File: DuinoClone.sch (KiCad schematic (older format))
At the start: 8 parts

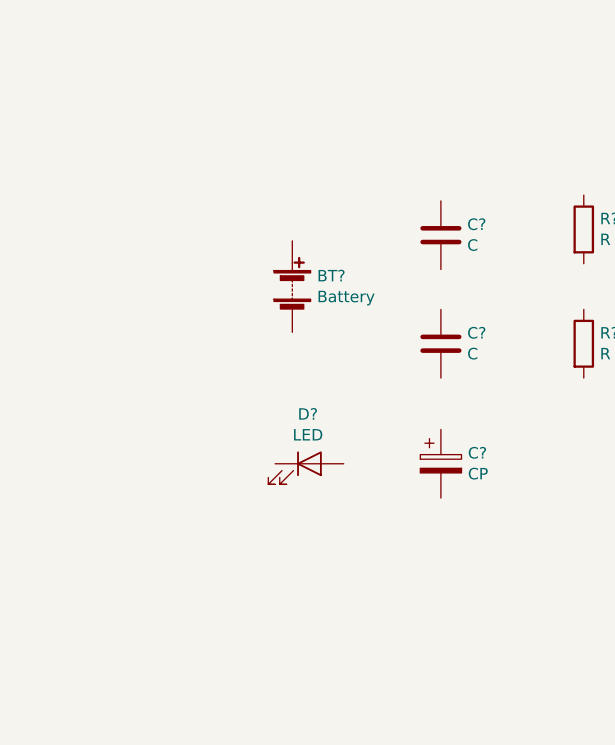
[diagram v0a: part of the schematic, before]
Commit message: Added symbol for Atmega328p-au
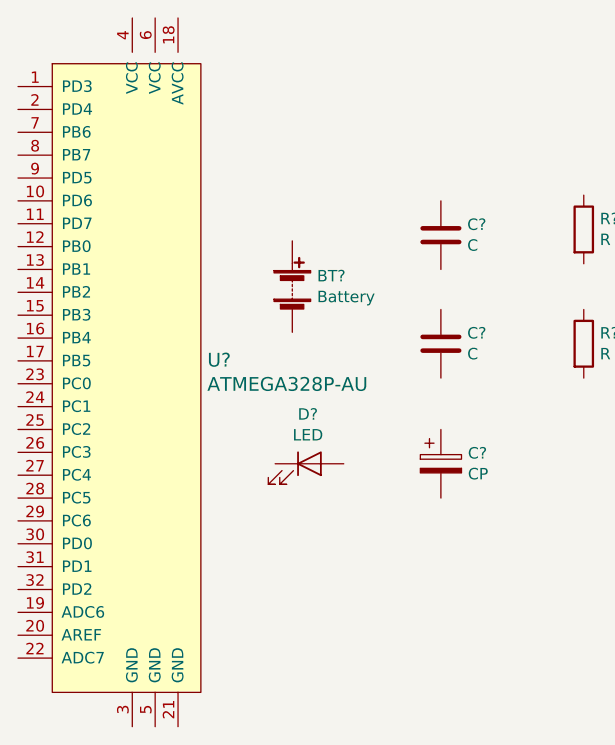
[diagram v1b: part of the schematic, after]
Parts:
- added U?: ATMEGA328P-AU, digikey-footprints:TQFP-32_7x7mm, symbol dk_Embedded-Microcontrollers:ATMEGA328P-AU
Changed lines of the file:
@@
 F1 "Connectors.sch" 50
 $EndSheet
+$Comp
+L dk_Embedded-Microcontrollers:ATMEGA328P-AU U?
+U 1 1 5CE4135D
+P 3975 4000
+F 0 "U?" H 4303 4103 60  0000 L CNN
+F 1 "ATMEGA328P-AU" H 4303 3997 60  0000 L CNN
+F 2 "digikey-footprints:TQFP-32_7x7mm" H 4175 4200 60  0001 L CNN
+F 3 "http://www.microchip.com/mymicrochip/filehandler.aspx?ddocname=en589968" H 4175 4300 60  0001 L CNN
+F 4 "ATMEGA328P-AU-ND" H 4175 4400 60  0001 L CNN "Digi-Key_PN"
+F 5 "ATMEGA328P-AU" H 4175 4500 60  0001 L CNN "MPN"
+F 6 "Integrated Circuits (ICs)" H 4175 4600 60  0001 L CNN "Category"
+F 7 "Embedded - Microcontrollers" H 4175 4700 60  0001 L CNN "Family"
+F 8 "http://www.microchip.com/mymicrochip/filehandler.aspx?ddocname=en589968" H 4175 4800 60  0001 L CNN "DK_Datasheet_Link"
+F 9 "/product-detail/en/microchip-technology/ATMEGA328P-AU/ATMEGA328P-AU-ND/1832260" H 4175 4900 60  0001 L CNN "DK_Detail_Page"
+F 10 "IC MCU 8BIT 32KB FLASH 32TQFP" H 4175 5000 60  0001 L CNN "Description"
+F 11 "Microchip Technology" H 4175 5100 60  0001 L CNN "Manufacturer"
+F 12 "Active" H 4175 5200 60  0001 L CNN "Status"
+	1    3975 4000
+	1    0    0    -1
+$EndComp
 $EndSCHEMATC

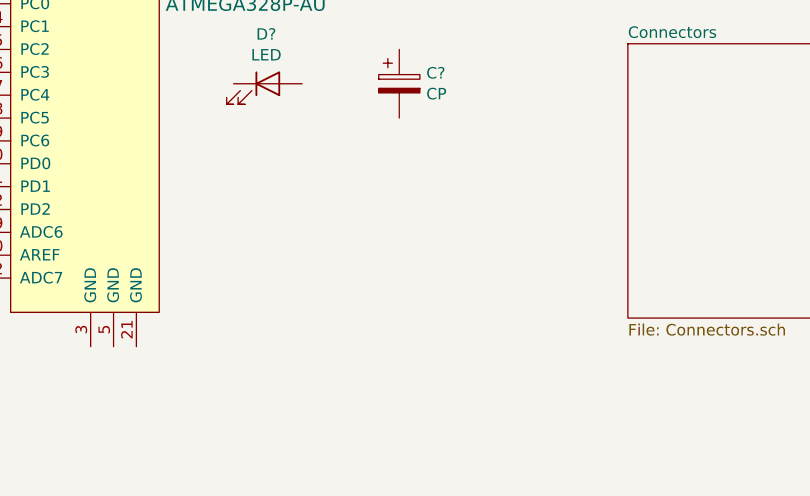
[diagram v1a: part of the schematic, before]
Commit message: Added clock IC custom symbol
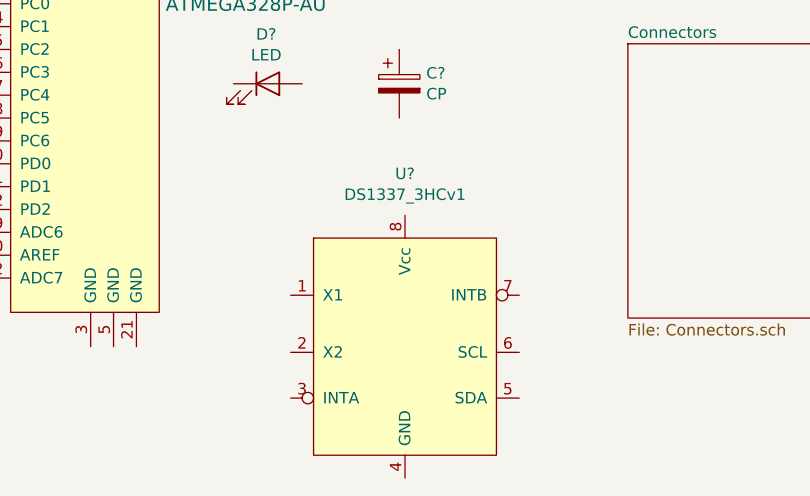
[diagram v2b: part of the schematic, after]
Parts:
- added U?: DS1337_3HCv1, symbol DuinoClone:DS1337_3HCv1
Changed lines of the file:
@@
+	1    0    0    -1
+$EndComp
+$Comp
+L DuinoClone:DS1337_3HCv1 U?
+U 1 1 5CE464AF
+P 5350 5475
+F 0 "U?" H 5350 6206 50  0000 C CNN
+F 1 "DS1337_3HCv1" H 5350 6115 50  0000 C CNN
+F 2 "" H 5700 6025 50  0001 C CNN
+F 3 "http://www.farnell.com/datasheets/74348.pdf" H 5700 6025 50  0001 C CNN
+	1    5350 5475
 	1    0    0    -1
 $EndComp

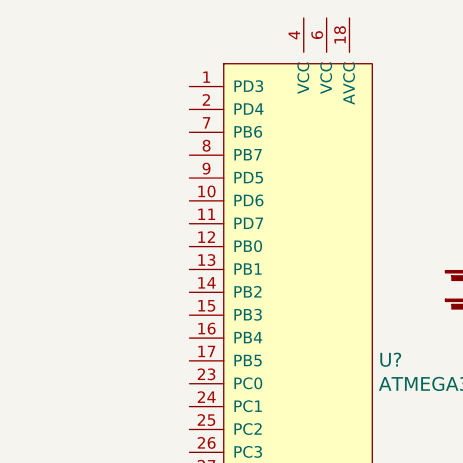
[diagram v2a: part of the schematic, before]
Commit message: Added crystal symbols to schematic
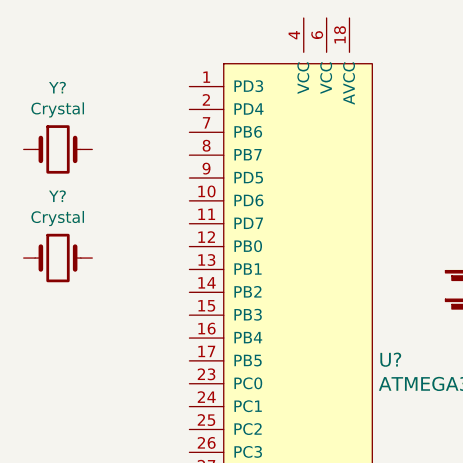
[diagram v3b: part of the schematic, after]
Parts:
- added Y? (x2): Crystal, symbol Device:Crystal
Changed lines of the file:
@@
+	1    0    0    -1
+$EndComp
+$Comp
+L Device:Crystal Y?
+U 1 1 5CE47483
+P 2900 2975
+F 0 "Y?" H 2900 3243 50  0000 C CNN
+F 1 "Crystal" H 2900 3152 50  0000 C CNN
+F 2 "" H 2900 2975 50  0001 C CNN
+F 3 "~" H 2900 2975 50  0001 C CNN
+	1    2900 2975
+	1    0    0    -1
+$EndComp
+$Comp
+L Device:Crystal Y?
+U 1 1 5CE4858A
+P 2900 3450
+F 0 "Y?" H 2900 3718 50  0000 C CNN
+F 1 "Crystal" H 2900 3627 50  0000 C CNN
+F 2 "" H 2900 3450 50  0001 C CNN
+F 3 "~" H 2900 3450 50  0001 C CNN
+	1    2900 3450
 	1    0    0    -1
 $EndComp

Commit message: Arranged symbols
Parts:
- added U?: 24LC1025, symbol Memory_EEPROM:24LC1025
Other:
- moved on the sheet: BT?, C?, D?, R?, U?, Y?
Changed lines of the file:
@@
 L Device:Battery BT?
 U 1 1 5CE2F41C
-P 4675 3575
-F 0 "BT?" H 4783 3621 50  0000 L CNN
-F 1 "Battery" H 4783 3530 50  0000 L CNN
-F 2 "" V 4675 3635 50  0001 C CNN
-F 3 "~" V 4675 3635 50  0001 C CNN
-	1    4675 3575
+P 8200 2275
+F 0 "BT?" H 8308 2321 50  0000 L CNN
+F 1 "Battery" H 8308 2230 50  0000 L CNN
+F 2 "" V 8200 2335 50  0001 C CNN
+F 3 "~" V 8200 2335 50  0001 C CNN
+	1    8200 2275
 	1    0    0    -1
 $EndComp
@@
 L Device:C C?
 U 1 1 5CE30EAD
-P 5325 3350
-F 0 "C?" H 5440 3396 50  0000 L CNN
-F 1 "C" H 5440 3305 50  0000 L CNN
-F 2 "" H 5363 3200 50  0001 C CNN
-F 3 "~" H 5325 3350 50  0001 C CNN
-	1    5325 3350
+P 4050 2400
+F 0 "C?" H 4165 2446 50  0000 L CNN
+F 1 "C" H 4165 2355 50  0000 L CNN
+F 2 "" H 4088 2250 50  0001 C CNN
+F 3 "~" H 4050 2400 50  0001 C CNN
+	1    4050 2400
 	1    0    0    -1
 $EndComp
@@
 L Device:C C?
 U 1 1 5CE31ACC
-P 5325 3825
-F 0 "C?" H 5440 3871 50  0000 L CNN
-F 1 "C" H 5440 3780 50  0000 L CNN
-F 2 "" H 5363 3675 50  0001 C CNN
-F 3 "~" H 5325 3825 50  0001 C CNN
-	1    5325 3825
+P 4050 2875
+F 0 "C?" H 4165 2921 50  0000 L CNN
+F 1 "C" H 4165 2830 50  0000 L CNN
+F 2 "" H 4088 2725 50  0001 C CNN
+F 3 "~" H 4050 2875 50  0001 C CNN
+	1    4050 2875
 	1    0    0    -1
 $EndComp
@@
 L Device:CP C?
 U 1 1 5CE322B6
-P 5325 4350
-F 0 "C?" H 5443 4396 50  0000 L CNN
-F 1 "CP" H 5443 4305 50  0000 L CNN
-F 2 "" H 5363 4200 50  0001 C CNN
-F 3 "~" H 5325 4350 50  0001 C CNN
-	1    5325 4350
+P 8525 3000
+F 0 "C?" H 8643 3046 50  0000 L CNN
+F 1 "CP" H 8643 2955 50  0000 L CNN
+F 2 "" H 8563 2850 50  0001 C CNN
+F 3 "~" H 8525 3000 50  0001 C CNN
+	1    8525 3000
 	1    0    0    -1
 $EndComp
@@
 L Device:LED D?
 U 1 1 5CE330B4
-P 4750 4350
-F 0 "D?" H 4743 4566 50  0000 C CNN
-F 1 "LED" H 4743 4475 50  0000 C CNN
-F 2 "" H 4750 4350 50  0001 C CNN
-F 3 "~" H 4750 4350 50  0001 C CNN
-	1    4750 4350
+P 4800 3275
+F 0 "D?" H 4793 3491 50  0000 C CNN
+F 1 "LED" H 4793 3400 50  0000 C CNN
+F 2 "" H 4800 3275 50  0001 C CNN
+F 3 "~" H 4800 3275 50  0001 C CNN
+	1    4800 3275
 	1    0    0    -1
 $EndComp
@@
 L Device:R R?
 U 1 1 5CE33F79
-P 5950 3325
-F 0 "R?" H 6020 3371 50  0000 L CNN
-F 1 "R" H 6020 3280 50  0000 L CNN
-F 2 "" V 5880 3325 50  0001 C CNN
-F 3 "~" H 5950 3325 50  0001 C CNN
-	1    5950 3325
+P 4275 3450
+F 0 "R?" H 4345 3496 50  0000 L CNN
+F 1 "R" H 4345 3405 50  0000 L CNN
+F 2 "" V 4205 3450 50  0001 C CNN
+F 3 "~" H 4275 3450 50  0001 C CNN
+	1    4275 3450
 	1    0    0    -1
 $EndComp
@@
 L Device:R R?
 U 1 1 5CE34AF5
-P 5950 3825
-F 0 "R?" H 6020 3871 50  0000 L CNN
-F 1 "R" H 6020 3780 50  0000 L CNN
-F 2 "" V 5880 3825 50  0001 C CNN
-F 3 "~" H 5950 3825 50  0001 C CNN
-	1    5950 3825
+P 4650 4775
+F 0 "R?" H 4720 4821 50  0000 L CNN
+F 1 "R" H 4720 4730 50  0000 L CNN
+F 2 "" V 4580 4775 50  0001 C CNN
+F 3 "~" H 4650 4775 50  0001 C CNN
+	1    4650 4775
 	1    0    0    -1
 $EndComp
@@
 L Memory_EEPROM:24LC1025 U?
 U 1 1 5CE35387
-P 6775 3400
-F 0 "U?" H 6775 3881 50  0000 C CNN
-F 1 "24LC1025" H 6775 3790 50  0000 C CNN
-F 2 "" H 6775 3400 50  0001 C CNN
-F 3 "http://ww1.microchip.com/downloads/en/DeviceDoc/21941B.pdf" H 6775 3400 50  0001 C CNN
-	1    6775 3400
+P 2400 4350
+F 0 "U?" H 2400 4831 50  0000 C CNN
+F 1 "24LC1025" H 2400 4740 50  0000 C CNN
+F 2 "" H 2400 4350 50  0001 C CNN
+F 3 "http://ww1.microchip.com/downloads/en/DeviceDoc/21941B.pdf" H 2400 4350 50  0001 C CNN
+	1    2400 4350
 	1    0    0    -1
 $EndComp
 $Sheet
-S 6325 4175 1100 1200
+S 3150 6175 1100 1200
 U 5CE3C2E7
 F0 "Connectors" 50
@@
 L dk_Embedded-Microcontrollers:ATMEGA328P-AU U?
 U 1 1 5CE4135D
-P 3975 4000
-F 0 "U?" H 4303 4103 60  0000 L CNN
-F 1 "ATMEGA328P-AU" H 4303 3997 60  0000 L CNN
-F 2 "digikey-footprints:TQFP-32_7x7mm" H 4175 4200 60  0001 L CNN
-F 3 "http://www.microchip.com/mymicrochip/filehandler.aspx?ddocname=en589968" H 4175 4300 60  0001 L CNN
-F 4 "ATMEGA328P-AU-ND" H 4175 4400 60  0001 L CNN "Digi-Key_PN"
-F 5 "ATMEGA328P-AU" H 4175 4500 60  0001 L CNN "MPN"
-F 6 "Integrated Circuits (ICs)" H 4175 4600 60  0001 L CNN "Category"
-F 7 "Embedded - Microcontrollers" H 4175 4700 60  0001 L CNN "Family"
-F 8 "http://www.microchip.com/mymicrochip/filehandler.aspx?ddocname=en589968" H 4175 4800 60  0001 L CNN "DK_Datasheet_Link"
-F 9 "/product-detail/en/microchip-technology/ATMEGA328P-AU/ATMEGA328P-AU-ND/1832260" H 4175 4900 60  0001 L CNN "DK_Detail_Page"
-F 10 "IC MCU 8BIT 32KB FLASH 32TQFP" H 4175 5000 60  0001 L CNN "Description"
-F 11 "Microchip Technology" H 4175 5100 60  0001 L CNN "Manufacturer"
-F 12 "Active" H 4175 5200 60  0001 L CNN "Status"
-	1    3975 4000
+P 6325 3575
+F 0 "U?" H 6653 3678 60  0000 L CNN
+F 1 "ATMEGA328P-AU" H 6653 3572 60  0000 L CNN
+F 2 "digikey-footprints:TQFP-32_7x7mm" H 6525 3775 60  0001 L CNN
+F 3 "http://www.microchip.com/mymicrochip/filehandler.aspx?ddocname=en589968" H 6525 3875 60  0001 L CNN
+F 4 "ATMEGA328P-AU-ND" H 6525 3975 60  0001 L CNN "Digi-Key_PN"
+F 5 "ATMEGA328P-AU" H 6525 4075 60  0001 L CNN "MPN"
+F 6 "Integrated Circuits (ICs)" H 6525 4175 60  0001 L CNN "Category"
+F 7 "Embedded - Microcontrollers" H 6525 4275 60  0001 L CNN "Family"
+F 8 "http://www.microchip.com/mymicrochip/filehandler.aspx?ddocname=en589968" H 6525 4375 60  0001 L CNN "DK_Datasheet_Link"
+F 9 "/product-detail/en/microchip-technology/ATMEGA328P-AU/ATMEGA328P-AU-ND/1832260" H 6525 4475 60  0001 L CNN "DK_Detail_Page"
+F 10 "IC MCU 8BIT 32KB FLASH 32TQFP" H 6525 4575 60  0001 L CNN "Description"
+F 11 "Microchip Technology" H 6525 4675 60  0001 L CNN "Manufacturer"
+F 12 "Active" H 6525 4775 60  0001 L CNN "Status"
+	1    6325 3575
 	1    0    0    -1
 $EndComp
@@
 L DuinoClone:DS1337_3HCv1 U?
 U 1 1 5CE464AF
-P 5350 5475
-F 0 "U?" H 5350 6206 50  0000 C CNN
-F 1 "DS1337_3HCv1" H 5350 6115 50  0000 C CNN
-F 2 "" H 5700 6025 50  0001 C CNN
-F 3 "http://www.farnell.com/datasheets/74348.pdf" H 5700 6025 50  0001 C CNN
-	1    5350 5475
+P 2325 2075
+F 0 "U?" H 2325 2806 50  0000 C CNN
+F 1 "DS1337_3HCv1" H 2325 2715 50  0000 C CNN
+F 2 "" H 2675 2625 50  0001 C CNN
+F 3 "http://www.farnell.com/datasheets/74348.pdf" H 2675 2625 50  0001 C CNN
+	1    2325 2075
 	1    0    0    -1
 $EndComp
@@
 L Device:Crystal Y?
 U 1 1 5CE47483
-P 2900 2975
-F 0 "Y?" H 2900 3243 50  0000 C CNN
-F 1 "Crystal" H 2900 3152 50  0000 C CNN
-F 2 "" H 2900 2975 50  0001 C CNN
-F 3 "~" H 2900 2975 50  0001 C CNN
-	1    2900 2975
+P 1475 1875
+F 0 "Y?" H 1475 2143 50  0000 C CNN
+F 1 "Crystal" H 1475 2052 50  0000 C CNN
+F 2 "" H 1475 1875 50  0001 C CNN
+F 3 "~" H 1475 1875 50  0001 C CNN
+	1    1475 1875
 	1    0    0    -1
 $EndComp
@@
 L Device:Crystal Y?
 U 1 1 5CE4858A
-P 2900 3450
-F 0 "Y?" H 2900 3718 50  0000 C CNN
-F 1 "Crystal" H 2900 3627 50  0000 C CNN
-F 2 "" H 2900 3450 50  0001 C CNN
-F 3 "~" H 2900 3450 50  0001 C CNN
-	1    2900 3450
+P 4675 2600
+F 0 "Y?" V 4629 2731 50  0000 L CNN
+F 1 "Crystal" V 4720 2731 50  0000 L CNN
+F 2 "" H 4675 2600 50  0001 C CNN
+F 3 "~" H 4675 2600 50  0001 C CNN
+	1    4675 2600
+	0    1    1    0
+$EndComp
+$Comp
+L Memory_EEPROM:24LC1025 U?
+U 1 1 5CE55027
+P 2400 5500
+F 0 "U?" H 2400 5981 50  0000 C CNN
+F 1 "24LC1025" H 2400 5890 50  0000 C CNN
+F 2 "" H 2400 5500 50  0001 C CNN
+F 3 "http://ww1.microchip.com/downloads/en/DeviceDoc/21941B.pdf" H 2400 5500 50  0001 C CNN
+	1    2400 5500
 	1    0    0    -1
 $EndComp
+$Comp
+L power:GND #PWR?
+U 1 1 5CE63FB2
+P 8525 3800
+F 0 "#PWR?" H 8525 3550 50  0001 C CNN
+F 1 "GND" H 8530 3627 50  0000 C CNN
+F 2 "" H 8525 3800 50  0001 C CNN
+F 3 "" H 8525 3800 50  0001 C CNN
+	1    8525 3800
+	1    0    0    -1
+$EndComp
